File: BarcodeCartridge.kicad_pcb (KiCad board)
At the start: 2 copper layers, 64.8 x 55.9 mm, 253 parts, among them J1 Cartridge Connector, J2 10103594-0001LF, M1 GM65-S, Q1 SMD-MOSFET-N-CH-20V-2.1A-CJ23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, Q2 SMD-MOSFET-P-CH-8V-4.1A-CJ230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, SW1 SW_Push, U1 W25Q128, U2 LP2985-33DBVR

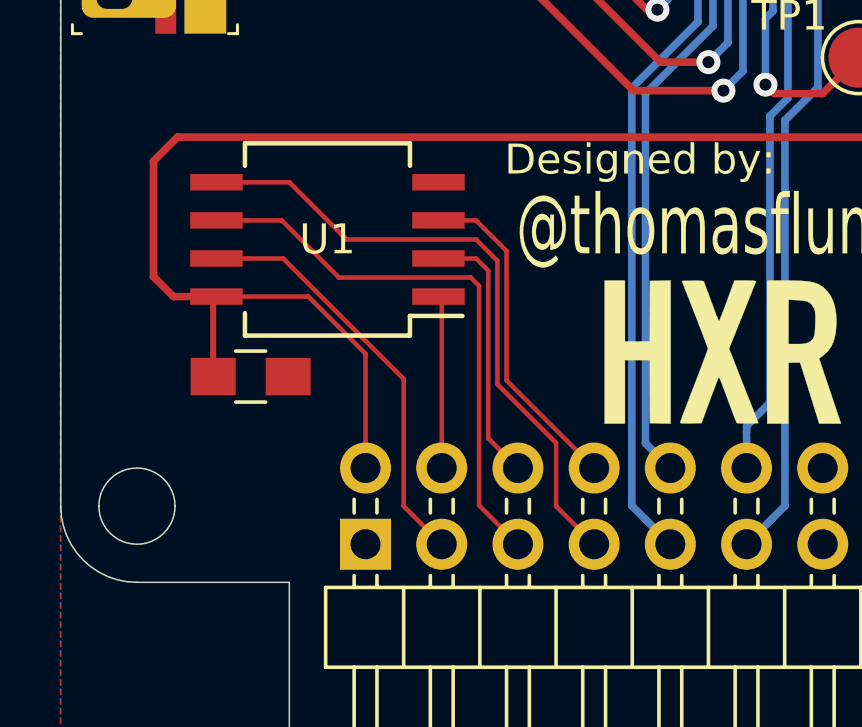
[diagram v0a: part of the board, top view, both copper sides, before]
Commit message: Fixed error in cartridge connector pin assignments
Updated to version 1.2
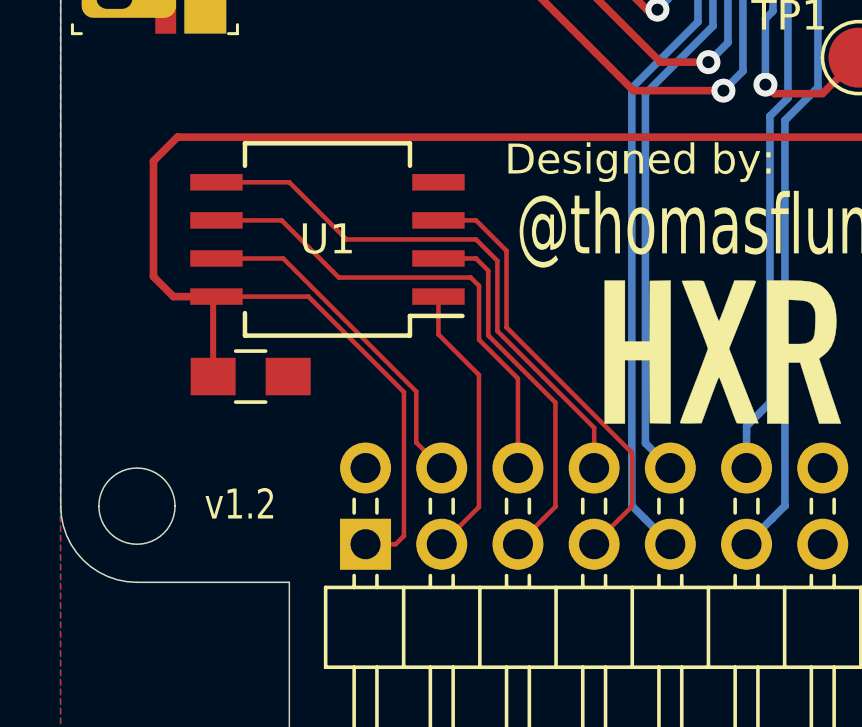
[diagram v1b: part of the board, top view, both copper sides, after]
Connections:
- J1 pad 1: GND -> +3V3
- J1 pad 2: +3V3 -> GND
- J1 pad 3: F_HOLD -> F_CS
- J1 pad 39: +5V -> +BATT
- J1 pad 4: F_CS -> F_HOLD
- J1 pad 40: +BATT -> +5V
- J1 pad 5: F_SCK -> F_MISO
- J1 pad 6: F_MISO -> F_SCK
- J1 pad 7: F_MOSI -> F_WP
- J1 pad 8: F_WP -> F_MOSI
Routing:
- net +3V3: track 57.8 -> 62.0 mm
- net F_CS: track 5.76 -> 9.48 mm
- net F_WP: track 11.1 -> 14.7 mm
- net F_MISO: track 8.82 -> 12.4 mm
- net F_MOSI: track 21.2 -> 18.7 mm
- net F_HOLD: track 13.9 -> 11.4 mm
- net F_SCK: track 18.8 -> 16.3 mm
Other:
- board text added: "v1.2"
